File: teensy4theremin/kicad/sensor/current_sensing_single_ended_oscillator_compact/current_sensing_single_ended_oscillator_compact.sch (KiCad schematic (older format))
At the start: 21 parts, among them J1 ANTENNA, J2 INDUCTOR_OUT, J3 INDUCTOR_IN, J6 OSC, U1 4220CZ6, U2 LD3985M33R_SOT23, U3 LT1711xMS8

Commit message: update pcb
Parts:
- added C13: 10nF, Capacitor_SMD:C_0805_2012Metric_Pad1.15x1.40mm_HandSolder, symbol Device:C
- added C14: 1nF, Capacitor_SMD:C_0805_2012Metric_Pad1.15x1.40mm_HandSolder, symbol Device:C
- added TP2: +3.3V, Connector_PinHeader_1.27mm:PinHeader_1x01_P1.27mm_Vertical, symbol Connector:TestPoint
- added TP3: GND, Connector_PinHeader_1.27mm:PinHeader_1x01_P1.27mm_Vertical, symbol Connector:TestPoint
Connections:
- net 3V3_A: now also C13.1, C14.1, TP2.1
- net GND: now also C13.2, C14.2, TP3.1
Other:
- moved on the sheet: C11, C9
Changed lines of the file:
@@
 Sheet 1 1
 Title "Theremin Oscillator"
-Date "2020-10-23"
-Rev "v1.1"
+Date "2020-10-24"
+Rev "v1.2"
 Comp ""
 Comment1 "Teensy 4 / FPGA Theremin Projects"
@@
 $EndComp
 Wire Wire Line
-	7750 3750 7150 3750
+	7750 3750 7250 3750
 Connection ~ 4100 4500
 Text Label 7400 3750 0    50   ~ 0
@@
 L power:GND #PWR015
 U 1 1 5F7D2E8E
-P 7150 3850
-F 0 "#PWR015" H 7150 3600 50  0001 C CNN
-F 1 "GND" H 7155 3677 50  0000 C CNN
-F 2 "" H 7150 3850 50  0001 C CNN
-F 3 "" H 7150 3850 50  0001 C CNN
-	1    7150 3850
-	1    0    0    -1
-$EndComp
-Wire Wire Line
-	7150 3750 7150 3850
+P 7250 3850
+F 0 "#PWR015" H 7250 3600 50  0001 C CNN
+F 1 "GND" H 7255 3677 50  0000 C CNN
+F 2 "" H 7250 3850 50  0001 C CNN
+F 3 "" H 7250 3850 50  0001 C CNN
+	1    7250 3850
+	1    0    0    -1
+$EndComp
+Wire Wire Line
+	7250 3750 7250 3850
 Wire Wire Line
 	4100 4900 4100 5000
@@
 Connection ~ 4900 1300
 NoConn ~ 3450 4300
-Text Label 6450 1300 0    50   ~ 0
+Text Label 5900 1300 0    50   ~ 0
 3V3_A
 $Comp
@@
 	5500 2750 5500 2300
 Wire Wire Line
-	5500 2300 6200 2300
-Wire Wire Line
-	6650 2300 6650 1300
+	5500 2300 6150 2300
+Wire Wire Line
+	6150 2300 6150 1300
 $Comp
 L Device:C C9
 U 1 1 5F99A62F
-P 6200 2500
-F 0 "C9" H 6315 2546 50  0000 L CNN
-F 1 "0.1uF" H 6315 2455 50  0000 L CNN
-F 2 "Capacitor_SMD:C_0805_2012Metric_Pad1.15x1.40mm_HandSolder" H 6238 2350 50  0001 C CNN
-F 3 "~" H 6200 2500 50  0001 C CNN
-	1    6200 2500
+P 6450 2500
+F 0 "C9" H 6565 2546 50  0000 L CNN
+F 1 "0.1uF" H 6565 2455 50  0000 L CNN
+F 2 "Capacitor_SMD:C_0805_2012Metric_Pad1.15x1.40mm_HandSolder" H 6488 2350 50  0001 C CNN
+F 3 "~" H 6450 2500 50  0001 C CNN
+	1    6450 2500
 	1    0    0    -1
 $EndComp
@@
 L power:GND #PWR07
 U 1 1 5F99B51E
-P 6200 2650
-F 0 "#PWR07" H 6200 2400 50  0001 C CNN
-F 1 "GND" H 6205 2477 50  0000 C CNN
-F 2 "" H 6200 2650 50  0001 C CNN
-F 3 "" H 6200 2650 50  0001 C CNN
-	1    6200 2650
+P 6450 2650
+F 0 "#PWR07" H 6450 2400 50  0001 C CNN
+F 1 "GND" H 6455 2477 50  0000 C CNN
+F 2 "" H 6450 2650 50  0001 C CNN
+F 3 "" H 6450 2650 50  0001 C CNN
+	1    6450 2650
 	1    0    0    -1
 $EndComp
@@
 L power:GND #PWR09
 U 1 1 5F99B92A
-P 6650 2650
-F 0 "#PWR09" H 6650 2400 50  0001 C CNN
-F 1 "GND" H 6655 2477 50  0000 C CNN
-F 2 "" H 6650 2650 50  0001 C CNN
-F 3 "" H 6650 2650 50  0001 C CNN
-	1    6650 2650
-	1    0    0    -1
-$EndComp
-Wire Wire Line
-	6650 2350 6650 2300
-Connection ~ 6650 2300
-Wire Wire Line
-	6200 2300 6200 2350
+P 6900 2650
+F 0 "#PWR09" H 6900 2400 50  0001 C CNN
+F 1 "GND" H 6905 2477 50  0000 C CNN
+F 2 "" H 6900 2650 50  0001 C CNN
+F 3 "" H 6900 2650 50  0001 C CNN
+	1    6900 2650
+	1    0    0    -1
+$EndComp
+Wire Wire Line
+	6900 2350 6900 2300
+Wire Wire Line
+	6450 2300 6450 2350
 $Comp
 L Device:CP C11
 U 1 1 5F9AC08F
-P 6650 2500
-F 0 "C11" H 6768 2546 50  0000 L CNN
-F 1 "4.7uF" H 6768 2455 50  0000 L CNN
-F 2 "Capacitor_Tantalum_SMD:CP_EIA-3528-21_Kemet-B_Pad1.50x2.35mm_HandSolder" H 6688 2350 50  0001 C CNN
-F 3 "~" H 6650 2500 50  0001 C CNN
-	1    6650 2500
+P 6900 2500
+F 0 "C11" H 7018 2546 50  0000 L CNN
+F 1 "4.7uF" H 7018 2455 50  0000 L CNN
+F 2 "Capacitor_Tantalum_SMD:CP_EIA-3528-21_Kemet-B_Pad1.50x2.35mm_HandSolder" H 6938 2350 50  0001 C CNN
+F 3 "~" H 6900 2500 50  0001 C CNN
+	1    6900 2500
 	1    0    0    -1
 $EndComp
@@
 Wire Wire Line
 	4600 4500 4600 4600
-Connection ~ 6200 2300
-Wire Wire Line
-	6200 2300 6650 2300
-Wire Wire Line
-	5850 1300 6650 1300
+Wire Wire Line
+	5850 1300 6150 1300
 $Comp
 L IP4220CZ6:IP4220CZ6 U1
@@
 	3100 1750 3650 1750
 Wire Wire Line
-	7150 750  7150 3550
-Wire Wire Line
-	7150 3550 7750 3550
+	7250 750  7250 3550
+Wire Wire Line
+	7250 3550 7750 3550
 NoConn ~ 3450 4700
 Wire Wire Line
@@
 	2200 3650 4500 3650
 Wire Wire Line
-	4750 750  7150 750
+	4750 750  7250 750
 Wire Wire Line
 	5900 2950 6900 2950
@@
 Wire Wire Line
 	2550 4500 2700 4500
+$Comp
+L Device:C C13
+U 1 1 5F95A9E4
+P 6450 1800
+F 0 "C13" H 6565 1846 50  0000 L CNN
+F 1 "10nF" H 6565 1755 50  0000 L CNN
+F 2 "Capacitor_SMD:C_0805_2012Metric_Pad1.15x1.40mm_HandSolder" H 6488 1650 50  0001 C CNN
+F 3 "~" H 6450 1800 50  0001 C CNN
+	1    6450 1800
+	1    0    0    -1
+$EndComp
+$Comp
+L power:GND #PWR0101
+U 1 1 5F95AC1E
+P 6450 1950
+F 0 "#PWR0101" H 6450 1700 50  0001 C CNN
+F 1 "GND" H 6455 1777 50  0000 C CNN
+F 2 "" H 6450 1950 50  0001 C CNN
+F 3 "" H 6450 1950 50  0001 C CNN
+	1    6450 1950
+	1    0    0    -1
+$EndComp
+$Comp
+L Device:C C14
+U 1 1 5F95DA73
+P 6900 1800
+F 0 "C14" H 7015 1846 50  0000 L CNN
+F 1 "1nF" H 7015 1755 50  0000 L CNN
+F 2 "Capacitor_SMD:C_0805_2012Metric_Pad1.15x1.40mm_HandSolder" H 6938 1650 50  0001 C CNN
+F 3 "~" H 6900 1800 50  0001 C CNN
+	1    6900 1800
+	1    0    0    -1
+$EndComp
+$Comp
+L power:GND #PWR0102
+U 1 1 5F95DCCB
+P 6900 1950
+F 0 "#PWR0102" H 6900 1700 50  0001 C CNN
+F 1 "GND" H 6905 1777 50  0000 C CNN
+F 2 "" H 6900 1950 50  0001 C CNN
+F 3 "" H 6900 1950 50  0001 C CNN
+	1    6900 1950
+	1    0    0    -1
+$EndComp
+Wire Wire Line
+	6900 1300 6900 1650
+Wire Wire Line
+	6450 1300 6450 1650
+Connection ~ 6450 1300
+Wire Wire Line
+	6450 1300 6900 1300
+Connection ~ 6450 2300
+Wire Wire Line
+	6450 2300 6900 2300
+Wire Wire Line
+	6150 2300 6450 2300
+Connection ~ 6150 2300
+Wire Wire Line
+	6150 1300 6450 1300
+Connection ~ 6150 1300
+$Comp
+L Connector:TestPoint TP2
+U 1 1 5F984E2F
+P 6900 1150
+F 0 "TP2" H 6958 1268 50  0000 L CNN
+F 1 "+3.3V" H 6958 1177 50  0000 L CNN
+F 2 "Connector_PinHeader_1.27mm:PinHeader_1x01_P1.27mm_Vertical" H 7100 1150 50  0001 C CNN
+F 3 "~" H 7100 1150 50  0001 C CNN
+	1    6900 1150
+	1    0    0    -1
+$EndComp
+Wire Wire Line
+	6900 1300 6900 1150
+Connection ~ 6900 1300
+$Comp
+L Connector:TestPoint TP3
+U 1 1 5F98A61F
+P 7700 1150
+F 0 "TP3" H 7758 1268 50  0000 L CNN
+F 1 "GND" H 7758 1177 50  0000 L CNN
+F 2 "Connector_PinHeader_1.27mm:PinHeader_1x01_P1.27mm_Vertical" H 7900 1150 50  0001 C CNN
+F 3 "~" H 7900 1150 50  0001 C CNN
+	1    7700 1150
+	1    0    0    -1
+$EndComp
+$Comp
+L power:GND #PWR01
+U 1 1 5F98A8CF
+P 7700 1400
+F 0 "#PWR01" H 7700 1150 50  0001 C CNN
+F 1 "GND" H 7705 1227 50  0000 C CNN
+F 2 "" H 7700 1400 50  0001 C CNN
+F 3 "" H 7700 1400 50  0001 C CNN
+	1    7700 1400
+	1    0    0    -1
+$EndComp
+Wire Wire Line
+	7700 1150 7700 1400
 $EndSCHEMATC

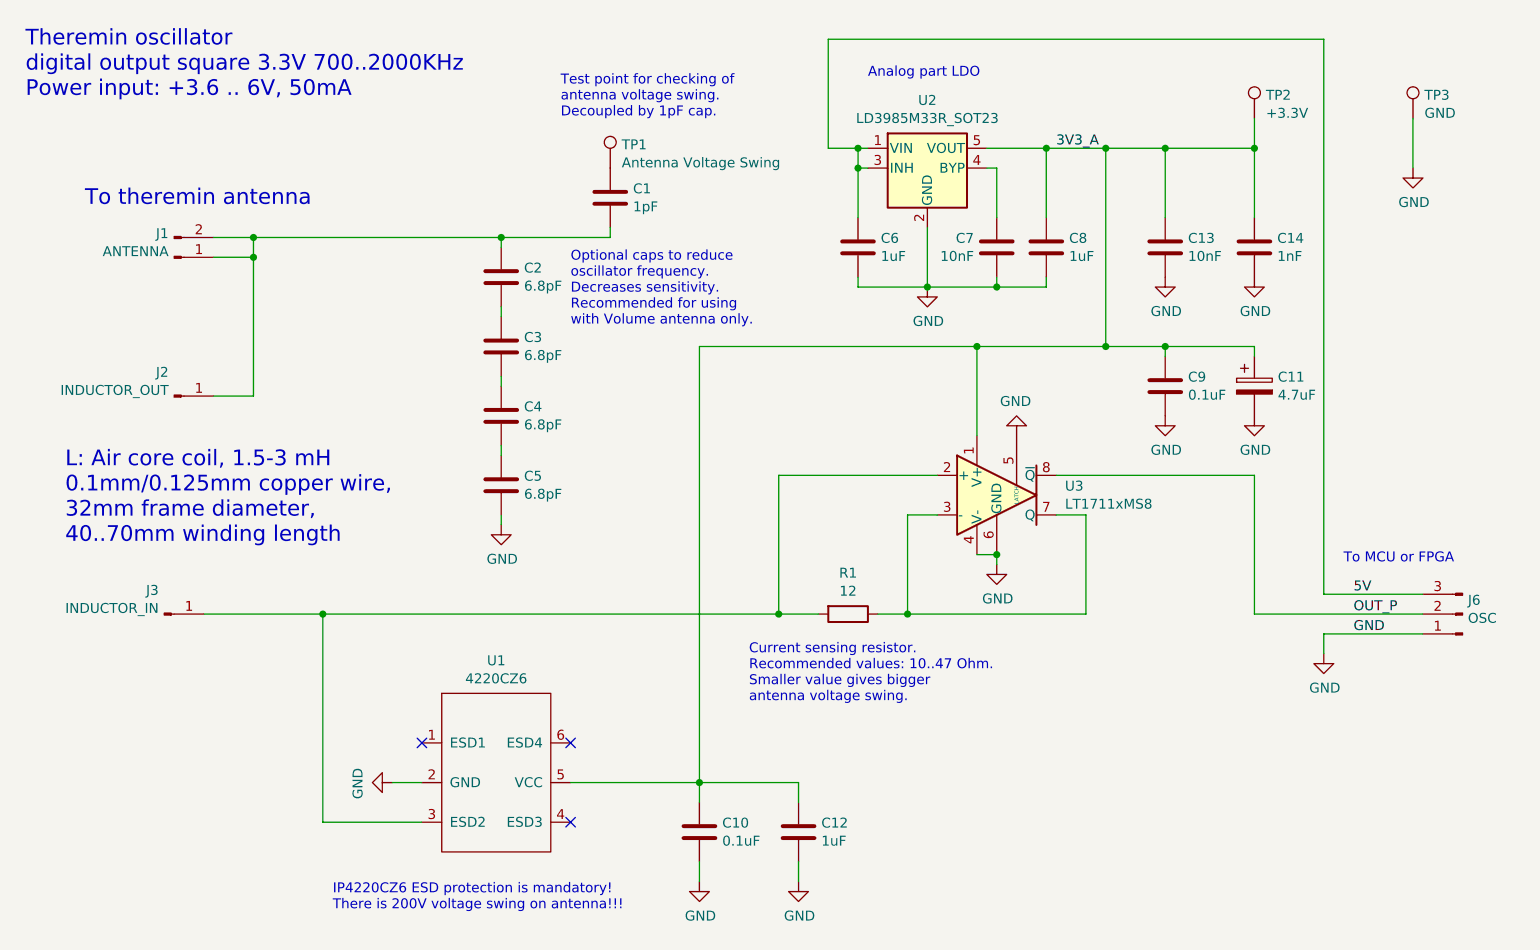
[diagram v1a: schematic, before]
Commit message: update oscillator pcb
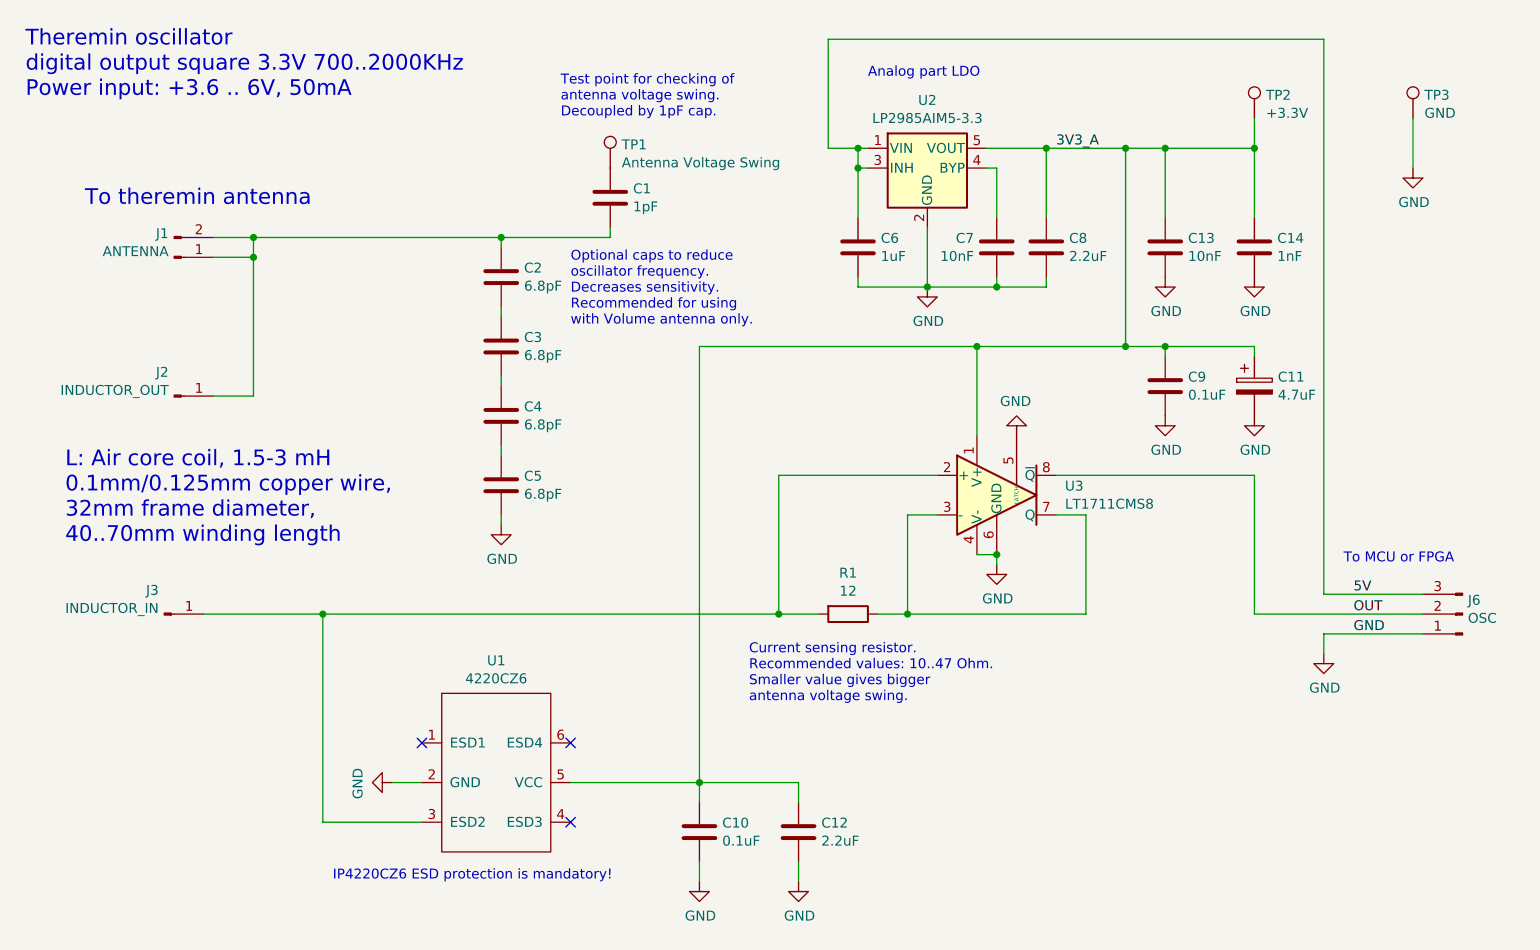
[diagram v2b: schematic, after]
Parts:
- C12, C8: value 1uF -> 2.2uF
- U2: value LD3985M33R_SOT23 -> LP2985AIM5-3.3
- U3: value LT1711xMS8 -> LT1711CMS8
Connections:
- net OUT_P renamed OUT
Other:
- note added: "IP4220CZ6 ESD protection is mandatory!"
- note removed: "IP4220CZ6 ESD protection is mandatory!\nThere is 200V voltage swing on antenna!!!"
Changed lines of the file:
@@
 	1    0    0    -1
 $EndComp
-Text Notes 2250 5150 0    50   ~ 0
-IP4220CZ6 ESD protection is mandatory!\nThere is 200V voltage swing on antenna!!!
+Text Notes 2250 5000 0    50   ~ 0
+IP4220CZ6 ESD protection is mandatory!
 Wire Wire Line
 	3450 4500 4100 4500
@@
 5V
 Text Label 7400 3650 0    50   ~ 0
-OUT_P
+OUT
 Wire Wire Line
 	4950 1400 4900 1400
@@
 P 5850 1800
 F 0 "C8" H 5965 1846 50  0000 L CNN
-F 1 "1uF" H 5965 1755 50  0000 L CNN
+F 1 "2.2uF" H 5965 1755 50  0000 L CNN
 F 2 "Capacitor_SMD:C_0805_2012Metric_Pad1.15x1.40mm_HandSolder" H 5888 1650 50  0001 C CNN
 F 3 "~" H 5850 1800 50  0001 C CNN
@@
 $EndComp
 Connection ~ 5850 1300
-$Comp
-L Regulator_Linear:LD3985M33R_SOT23 U2
-U 1 1 5F6A75CD
-P 5250 1400
-F 0 "U2" H 5250 1742 50  0000 C CNN
-F 1 "LD3985M33R_SOT23" H 5250 1651 50  0000 C CNN
-F 2 "Package_TO_SOT_SMD:SOT-23-5" H 5250 1725 50  0001 C CIN
-F 3 "http://www.st.com/internet/com/TECHNICAL_RESOURCES/TECHNICAL_LITERATURE/DATASHEET/CD00003395.pdf" H 5250 1400 50  0001 C CNN
-	1    5250 1400
-	1    0    0    -1
-$EndComp
 Wire Wire Line
 	5550 1400 5600 1400
@@
 P 5600 3050
 F 0 "U3" H 5944 3096 50  0000 L CNN
-F 1 "LT1711xMS8" H 5944 3005 50  0000 L CNN
+F 1 "LT1711CMS8" H 5944 3005 50  0000 L CNN
 F 2 "Package_SO:MSOP-8_3x3mm_P0.65mm" H 5600 2650 50  0001 C CNN
 F 3 "https://www.analog.com/media/en/technical-documentation/data-sheets/171112f.pdf" H 5600 3050 50  0001 C CNN
@@
 	5500 2750 5500 2300
 Wire Wire Line
-	5500 2300 6150 2300
-Wire Wire Line
-	6150 2300 6150 1300
+	6250 2300 6250 1300
 $Comp
 L Device:C C9
@@
 P 4600 4750
 F 0 "C12" H 4715 4796 50  0000 L CNN
-F 1 "1uF" H 4715 4705 50  0000 L CNN
+F 1 "2.2uF" H 4715 4705 50  0000 L CNN
 F 2 "Capacitor_SMD:C_0805_2012Metric_Pad1.15x1.40mm_HandSolder" H 4638 4600 50  0001 C CNN
 F 3 "~" H 4600 4750 50  0001 C CNN
@@
 Wire Wire Line
 	4600 4500 4600 4600
-Wire Wire Line
-	5850 1300 6150 1300
 $Comp
 L IP4220CZ6:IP4220CZ6 U1
@@
 Wire Wire Line
 	6450 2300 6900 2300
-Wire Wire Line
-	6150 2300 6450 2300
-Connection ~ 6150 2300
-Wire Wire Line
-	6150 1300 6450 1300
-Connection ~ 6150 1300
 $Comp
 L Connector:TestPoint TP2
@@
 Wire Wire Line
 	7700 1150 7700 1400
+Connection ~ 6250 1300
+Wire Wire Line
+	6250 1300 6450 1300
+Connection ~ 6250 2300
+Wire Wire Line
+	6250 2300 6450 2300
+Wire Wire Line
+	5500 2300 6250 2300
+Wire Wire Line
+	5850 1300 6250 1300
+$Comp
+L Regulator_Linear:LD3985M33R_SOT23 U2
+U 1 1 5F6A75CD
+P 5250 1400
+F 0 "U2" H 5250 1742 50  0000 C CNN
+F 1 "LP2985AIM5-3.3" H 5250 1651 50  0000 C CNN
+F 2 "Package_TO_SOT_SMD:SOT-23-5" H 5250 1725 50  0001 C CIN
+F 3 "http://www.st.com/internet/com/TECHNICAL_RESOURCES/TECHNICAL_LITERATURE/DATASHEET/CD00003395.pdf" H 5250 1400 50  0001 C CNN
+	1    5250 1400
+	1    0    0    -1
+$EndComp
 $EndSCHEMATC
